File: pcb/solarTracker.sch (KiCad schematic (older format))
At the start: 29 parts, among them U1 74HC4052, U2 STM32F071CBT6

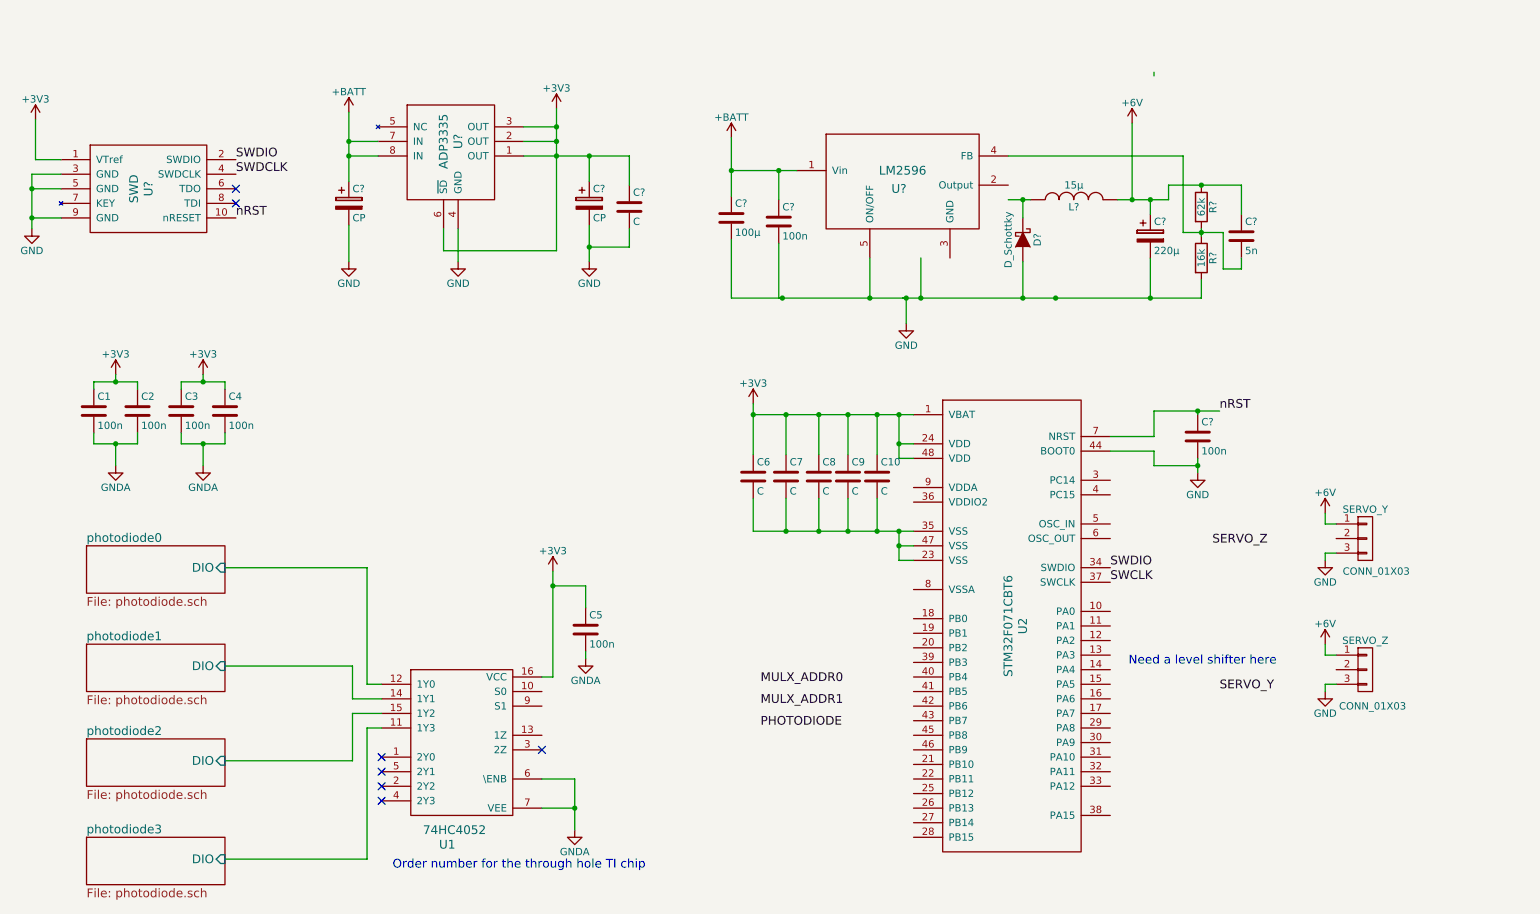
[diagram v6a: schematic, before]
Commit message: connect mcu to servo and mux, add level shifter
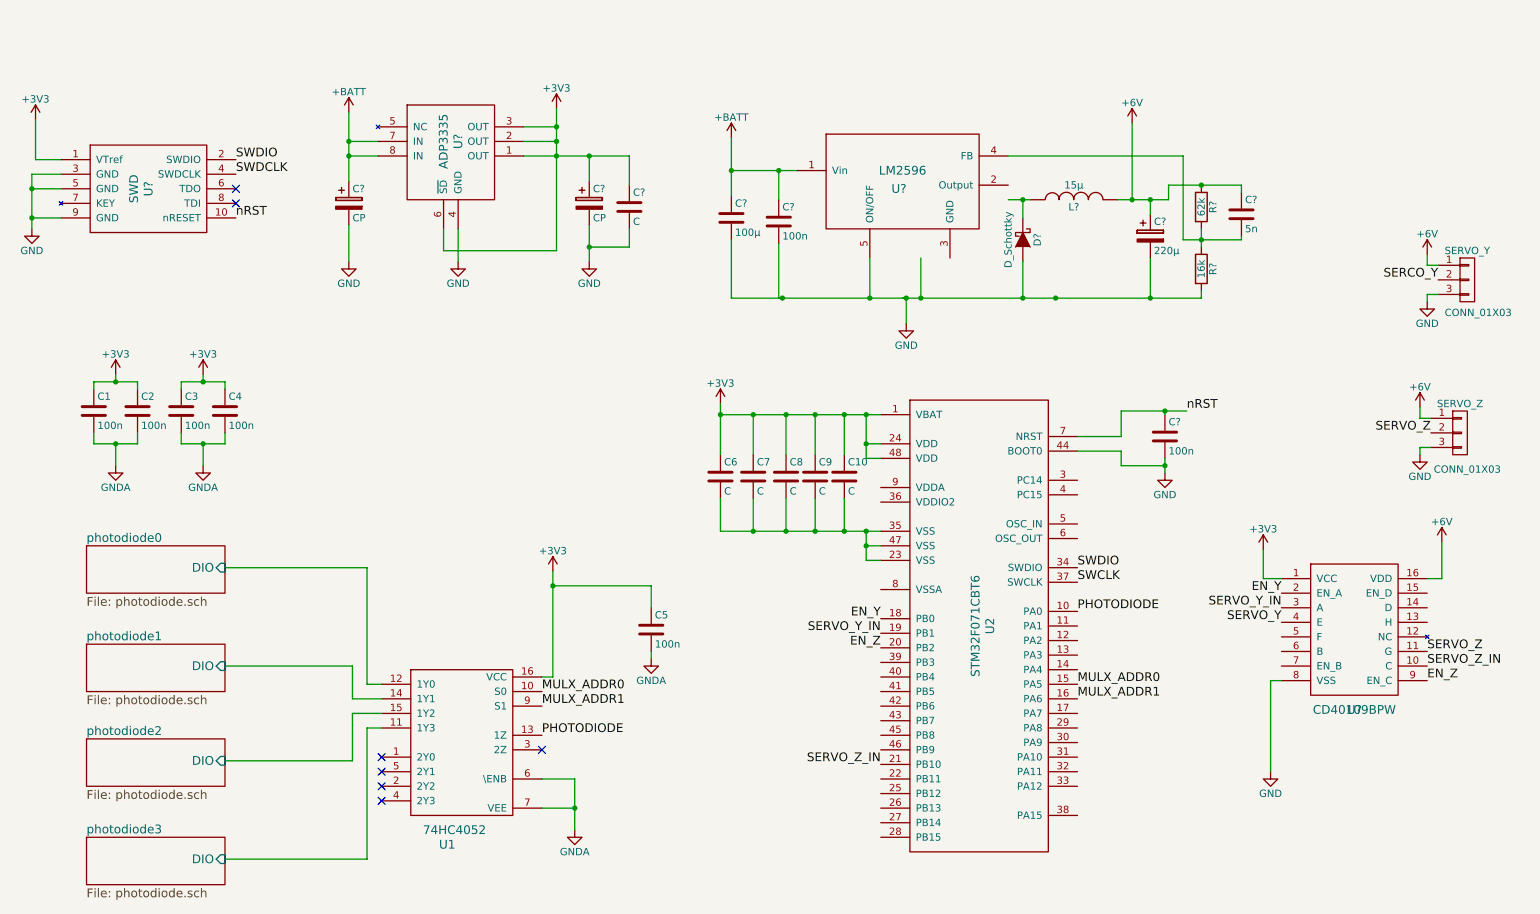
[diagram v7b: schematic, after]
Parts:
- added U?: CD40109BPW, symbol CD40109BPW
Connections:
- net labels added: EN_Y, EN_Z, SERCO_Y, SERVO_Y_IN, SERVO_Z_IN
- wire segments 122 -> 125
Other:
- note removed: "Need a level shifter here\n"
- note removed: "Order number for the through hole TI chip"
- moved on the sheet: C10, C5, C6, C7, C8, C9, C?, R?, SERVO_Y, SERVO_Z, U2

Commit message: change BATT to 3V3 regulator
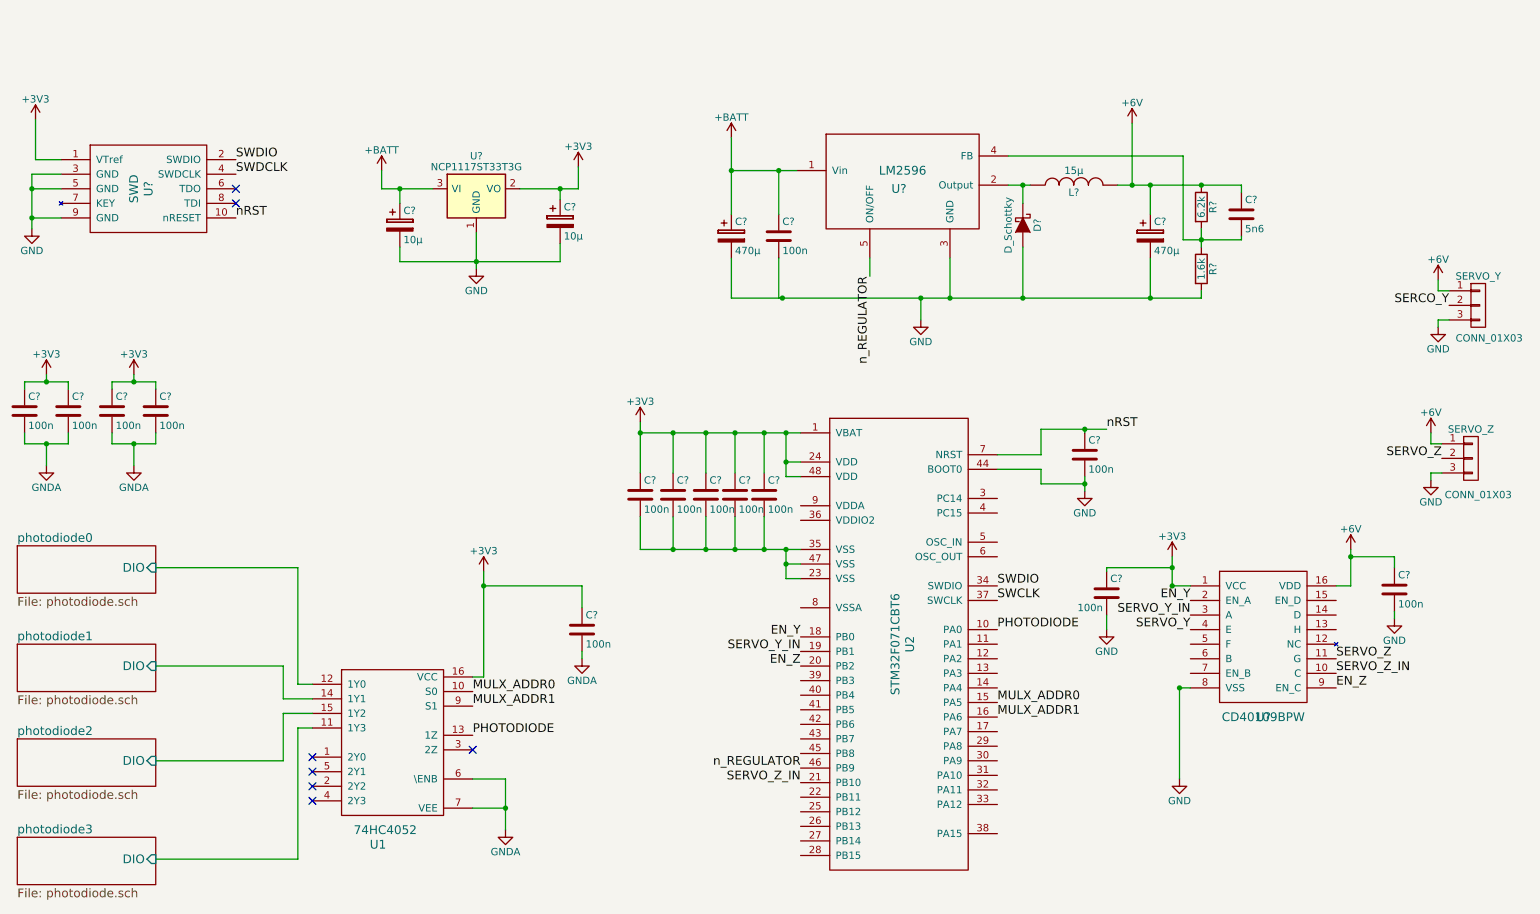
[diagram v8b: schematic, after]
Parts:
- removed C1, C2, C3, C4, C5, C?: 100n, symbol C
- removed C10, C6, C7, C8, C9, C?: C, symbol C
- removed C? (x2): CP, symbol CP
- removed C?: 100µ, symbol C
- removed U?: ADP3335, symbol ADP3335
- added C?: 470µ, symbol CP
- added C? (x13): 100n, symbol C
- added C? (x2): 10µ, symbol CP
- added U?: NCP1117ST33T3G, TO_SOT_Packages_SMD:SOT-223, symbol NCP1117ST33T3G
- C?: value 220µ -> 470µ; Farnell Code 1890582 -> (none); Order No (none) -> 1219483; Supplier (none) -> Farnell
- C?: value 5n -> 5n6; Order No (none) -> 2471760; Supplier (none) -> Farnell
- C?: Order No (none) -> 2496944; Supplier (none) -> Farnell
- D?: Order No (none) -> 9381392; Supplier (none) -> Farnell
- L?: Order No (none) -> 2215912; Supplier (none) -> Farnell
- R?: value 62k -> 6.2k; Order No (none) -> 2323860; Supplier (none) -> Farnell
- R?: value 16k -> 1.6k; Order No (none) -> 9332669; Supplier (none) -> Farnell
- U?: Order No (none) -> 1469194; Supplier (none) -> Farnell
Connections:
- net +3V3: now also C?.1, C?.1, C?.1, C?.1, C?.1, C?.1, C?.1, C?.1, C?.1, C?.1, C?.1, C?.1, U?.2 (VO)
- net +6V: now also C?.1
- net +BATT: now also C?.1, C?.1, U?.3 (VI)
- net GND: now also U?.3 (GND), C?.2, C?.2, C?.2, C?.2, C?.2, C?.2, U?.1 (GND); no longer C?.2, U?.5 (ON/OFF)
- net GNDA: now also C?.2, C?.2, C?.2, C?.2, C?.2
- net nRST: now also C?.1
- net at U2.23 (VSS), U2.35 (VSS), U2.47 (VSS): now also C?.2, C?.2, C?.2, C?.2, C?.2
- net n_REGULATOR: now reaches U2.46 (PB9)
- net n_REGULATOR: now also U?.5 (ON/OFF)
- net at U?.2 (Output): now also D?.1 (K), L?.1
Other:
- moved on the sheet: C?, D?, L?, SERVO_Y, SERVO_Z, U1, U2, U?
